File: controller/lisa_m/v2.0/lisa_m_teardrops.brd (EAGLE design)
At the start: 50.7 x 33.6 mm, 119 parts, among them IC9 LP2992 5V, J1 CONN_3-1, J2 CONN_3-1, J3 CONN_3-1, J4 CONN_3-1, J5 CONN_3-1, J6 CONN_3-1, J7 CONN_3-1, J8 CONN_3-1, Q1 12Mhz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

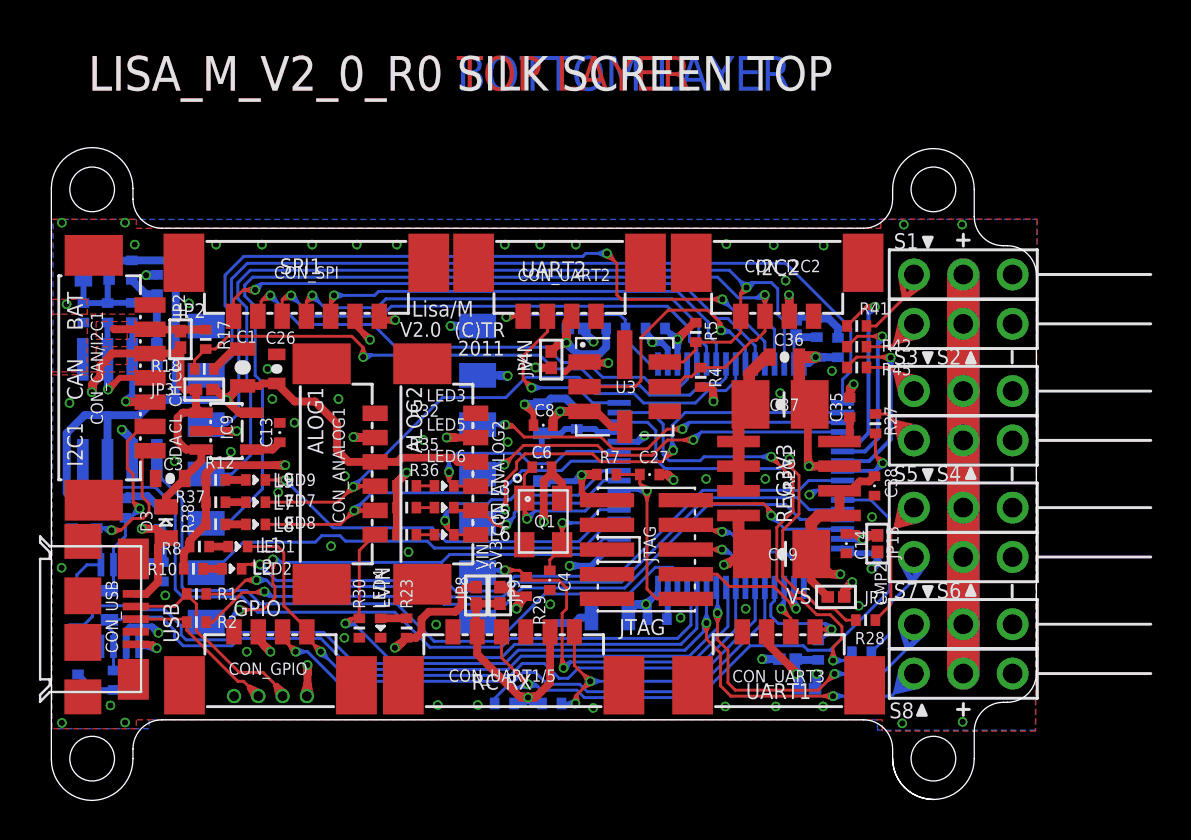
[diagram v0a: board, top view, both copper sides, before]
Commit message: Updated led footprints to have placement information about orientation.
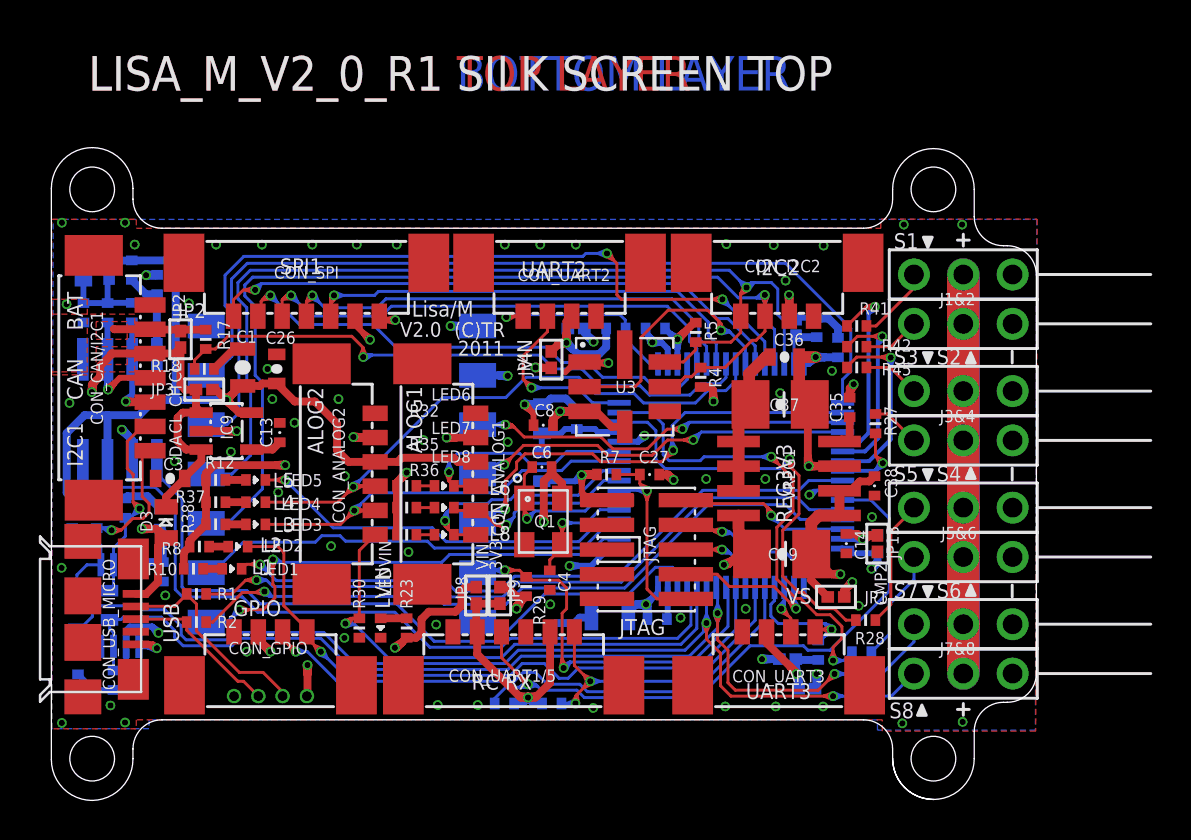
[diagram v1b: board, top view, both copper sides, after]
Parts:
- removed LED9: BLU, pel_dipol_comp:0402-LED
- added LEDVIN: GRN, pel_dipol_comp:0402-LED
- C4, C6: value 30p -> 10p
- LED2, LED3, LED5: value BLU -> GRN
- LED4: value ORG -> RED
- R1, R2: value 22R -> 0R
- R10, R12, R37, R38: value 80R -> 300
- R18, R23: value 2k -> 2k2
- R24, R26, R29, R3, R30, R6: value 2k7 -> 10k
- R33, R34, R4, R5: value 2k7 -> 2k2
- R43, R44: value 1k5 -> 2k2
- R8: value 300R -> 300
- moved LED3 9.90 mm to (10.5, 10.1), turned to 180 degrees
- moved LED5 9.81 mm to (10.5, 12.3), turned to 180 degrees
- moved LED8 9.72 mm to (20.2, 9.53), turned to 180 degrees
- moved LED7 9.71 mm to (20.2, 10.9), turned to 180 degrees
- moved LED4 9.13 mm to (10.5, 11.2), turned to 180 degrees
- moved CON_ANALOG1 5.18 mm to (20.6, 12.6)
- moved CON_ANALOG2 5.18 mm to (15.4, 12.6)
- moved LED6 2.51 mm to (20.2, 12.0), turned to 180 degrees
- moved LED1 1.18 mm to (9.30, 7.77), turned to 180 degrees
- moved LED2 1.18 mm to (9.60, 8.92), turned to 180 degrees
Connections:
- net ADC_1: now also CON_ANALOG1.4, LED6.C; no longer CON_ANALOG2.4, LED3.C
- net ADC_2: now also CON_ANALOG1.5, LED7.C; no longer CON_ANALOG2.5, LED5.C
- net ADC_3: now also CON_ANALOG1.6, LED8.C; no longer CON_ANALOG2.6, LED6.C
- net ADC_4: now also CON_ANALOG2.4, LED4.C; no longer CON_ANALOG1.4, LED7.C
- net ADC_6: now also CON_ANALOG2.5, LED3.C; no longer CON_ANALOG1.5, LED8.C
- net BOOT0: now also CON_ANALOG2.6; no longer CON_ANALOG1.6
- net GND: now also LEDVIN.C; no longer LED4.C
- net JTAG_TRST: now also LED2.C; no longer LED1.C
- net LED1: now also LED1.C; no longer LED2.C
- net LED2: now also LED5.C; no longer LED9.C
- net N$10: now also LED2.A; no longer LED1.A
- net N$11: now also LED8.A; no longer LED6.A
- net N$12: now also LEDVIN.A; no longer LED4.A
- net N$13: now also LED5.A; no longer LED9.A
- net N$14: now also LED4.A; no longer LED7.A
- net N$15: now also LED3.A; no longer LED8.A
- net N$4: now also LED1.A; no longer LED2.A
- net N$5: now also LED6.A; no longer LED3.A
- net N$9: now also LED7.A; no longer LED5.A
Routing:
- net S4: track 6.04 -> 2.54 mm
- net S3: track 6.45 -> 2.95 mm
- net S1: track 7.45 -> 3.95 mm
- net S2: track 6.43 -> 2.93 mm
- net S8: track 6.27 -> 2.77 mm
- net S7: track 7.31 -> 3.81 mm
- net S5: track 10.1 -> 6.61 mm
- net S6: track 9.31 -> 5.81 mm
- net SERVO_BUS: track 77.5 -> 74.0 mm
- net FT_USB_DM: track 12.6 -> 10.9 mm
- net FT_USB_DP: track 9.80 -> 8.19 mm
- net USB_VBUS: track 70.3 -> 68.8 mm
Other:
- board text added: "CON_USB_MICRO"
- board text added: "J1&2"
- board text added: "J3&4"
- board text added: "J5&6"
- board text added: "J7&8"
- board text added: "L4"
- board text added: "LISA_M_V2_0_R1 BOTTOM LAYER"
- board text added: "LISA_M_V2_0_R1 LAYER 2"
- board text added: "LISA_M_V2_0_R1 LAYER 3"
- board text added: "LISA_M_V2_0_R1 SILK SCREEN BOTTOM"
- board text added: "LISA_M_V2_0_R1 SILK SCREEN TOP"
- board text added: "LISA_M_V2_0_R1 TOP LAYER"
- board text added: "RX1"
- board text added: "UART3"
- board text removed: "CON_USB"
- board text removed: "L9"
- board text removed: "LISA_M_V2_0_R0 BOTTOM LAYER"
- board text removed: "LISA_M_V2_0_R0 LAYER 2"
- board text removed: "LISA_M_V2_0_R0 LAYER 3"
- board text removed: "LISA_M_V2_0_R0 SILK SCREEN BOTTOM"
- board text removed: "LISA_M_V2_0_R0 SILK SCREEN TOP"
- board text removed: "LISA_M_V2_0_R0 TOP LAYER"
- board text removed: "RX3"
- board text removed: "UART1"
